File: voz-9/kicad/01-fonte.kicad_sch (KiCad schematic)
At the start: 0 parts

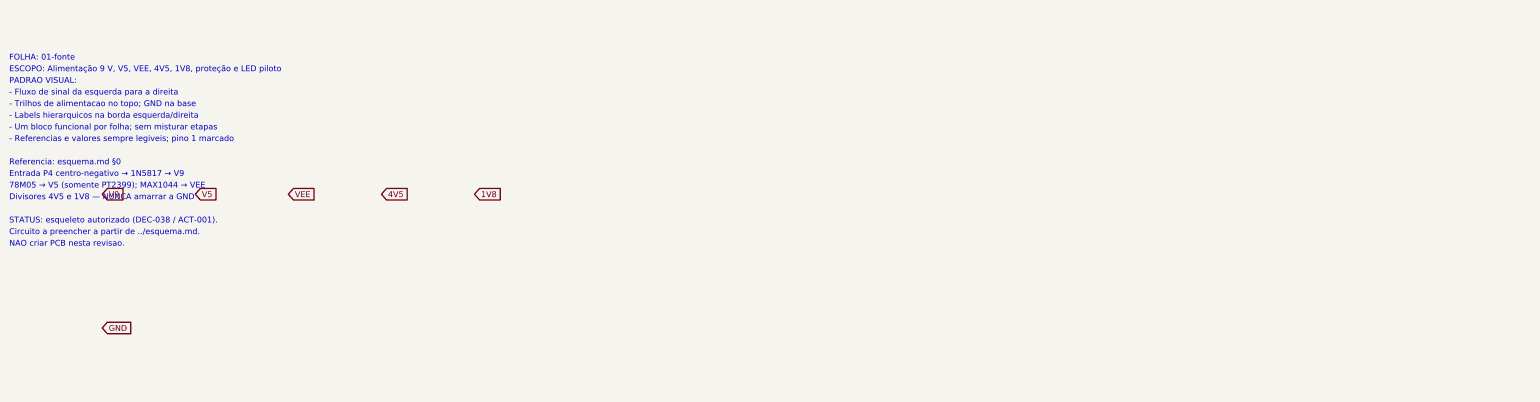
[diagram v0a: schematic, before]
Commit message: feat: install Konnect and capture power sheet
Add Konnect MCP config/client for realtime schematic edits, document
KiCad 10 realtime viewing, and fill 01-fonte from esquema.md §0 with
validated connectivity (no PCB).

Co-authored-by: Andrey <andreysenes@users.noreply.github.com>
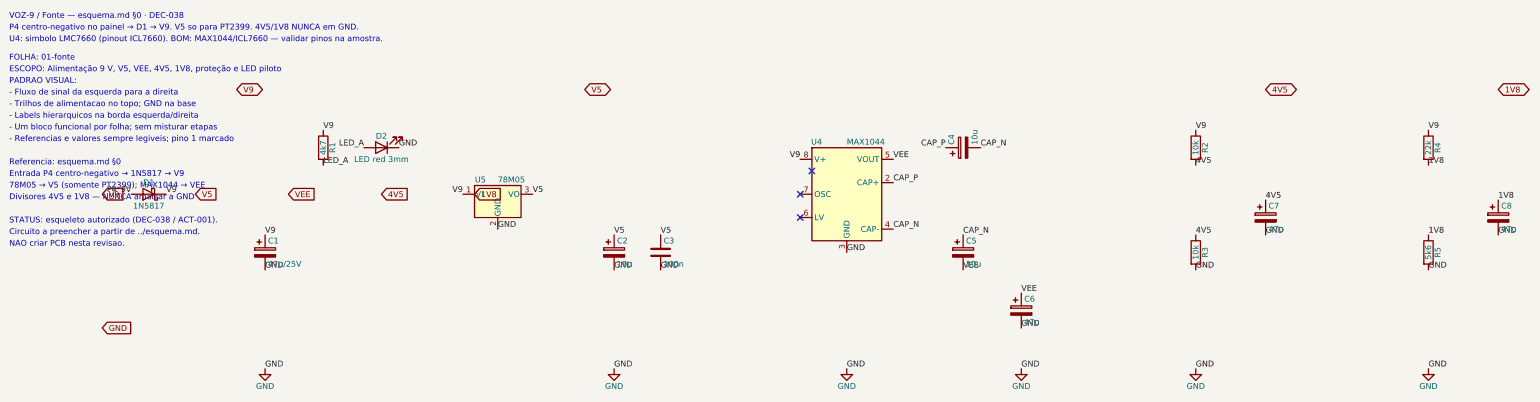
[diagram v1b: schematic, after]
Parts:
- added C1: 47u/25V, symbol Device:C_Polarized
- added C2, C4, C5: 10u, symbol Device:C_Polarized
- added C3: 100n, symbol Device:C
- added C6, C7, C8: 47u, symbol Device:C_Polarized
- added D1: 1N5817, Diode_THT:D_DO-41_SOD81_P10.16mm_Horizontal, symbol Diode:1N5817
- added D2: LED red 3mm, symbol Device:LED
- added R1: 4k7, symbol Device:R
- added R2, R3: 10k, symbol Device:R
- added R4: 22k, symbol Device:R
- added R5: 5k6, symbol Device:R
- added U4: MAX1044, symbol Regulator_SwitchedCapacitor:LMC7660
- added U5: 78M05, Package_TO_SOT_THT:TO-220-3_Vertical, symbol Regulator_Linear:LM78M05_TO220
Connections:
- net 1V8: now also C8.1, R4.2, R5.1
- net 4V5: now also C7.1, R2.2, R3.1
- net GND: now also C1.2, C2.2, C3.2, C6.2, C7.2, C8.2, D2.1 (K), R3.2, R5.2, U4.3 (GND), U5.2 (GND)
- net V5: now also C2.1, C3.1, U5.3 (VO)
- net V9: now also C1.1, D1.1 (K), R1.1, R2.1, R4.1, U4.8 (V+), U5.1 (VI)
- net VEE: now also C5.2, C6.1, U4.5 (VOUT)
- new net CAP_N: C4.2, C5.1, U4.4 (CAP-)
- new net CAP_P: C4.1, U4.2 (CAP+)
- new net LED_A: D2.2 (A), R1.2
- new net P4_9V: D1.2 (A)
- no-connect marks 0 -> 3
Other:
- note added: "P4 centro-negativo no painel → D1 → V9. V5 so para PT2399. 4V5/1V8 NUNCA em GND."
- note added: "U4: simbolo LMC7660 (pinout ICL7660). BOM: MAX1044/ICL7660 — validar pinos na amostra."
- note added: "VOZ-9 / Fonte — esquema.md §0 · DEC-038"
